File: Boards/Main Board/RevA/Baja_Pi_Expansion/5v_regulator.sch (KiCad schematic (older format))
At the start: 3 parts

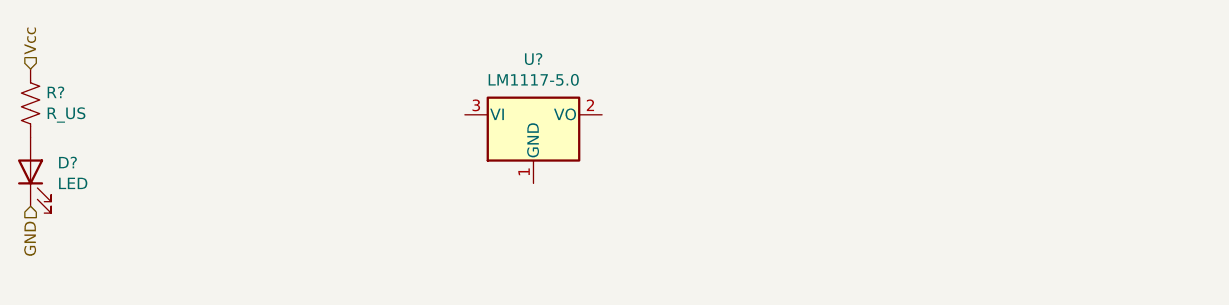
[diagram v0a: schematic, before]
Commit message: Added 5V Regulator Schematic
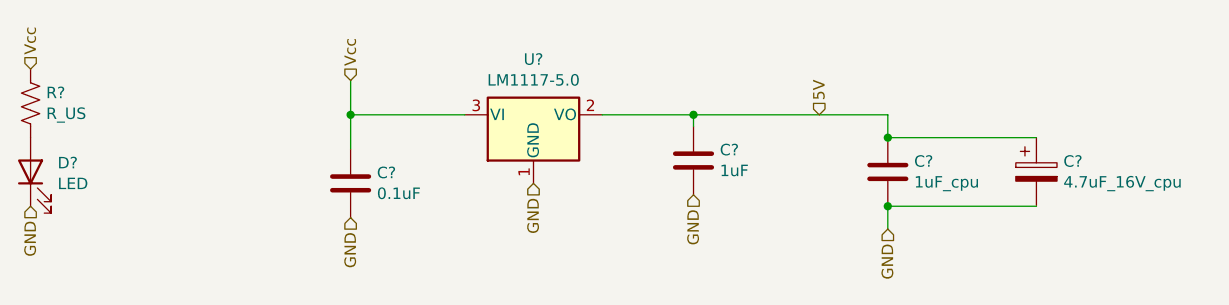
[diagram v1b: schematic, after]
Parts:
- added C?: 0.1uF, symbol Device:C
- added C?: 1uF, symbol Device:C
- added C?: 1uF_cpu, symbol Device:C
- added C?: 4.7uF_16V_cpu, symbol Device:CP
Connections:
- net GND: now also U?.1 (GND), C?.2, C?.2, C?.2, C?.2
- net Vcc: now also U?.3 (VI), C?.1
- net 5V: now reaches U?.2 (VO)
- net 5V: now also C?.1, C?.1, C?.1
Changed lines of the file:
@@
 	1    0    0    -1
 $EndComp
+$Comp
+L Device:C C?
+U 1 1 61655F33
+P 3950 3150
+F 0 "C?" H 4065 3196 50  0000 L CNN
+F 1 "0.1uF" H 4065 3105 50  0000 L CNN
+F 2 "" H 3988 3000 50  0001 C CNN
+F 3 "~" H 3950 3150 50  0001 C CNN
+	1    3950 3150
+	1    0    0    -1
+$EndComp
+$Comp
+L Device:C C?
+U 1 1 61656877
+P 5450 3050
+F 0 "C?" H 5565 3096 50  0000 L CNN
+F 1 "1uF" H 5565 3005 50  0000 L CNN
+F 2 "" H 5488 2900 50  0001 C CNN
+F 3 "~" H 5450 3050 50  0001 C CNN
+	1    5450 3050
+	1    0    0    -1
+$EndComp
+$Comp
+L Device:C C?
+U 1 1 6165740F
+P 6300 3100
+F 0 "C?" H 6415 3146 50  0000 L CNN
+F 1 "1uF_cpu" H 6415 3055 50  0000 L CNN
+F 2 "" H 6338 2950 50  0001 C CNN
+F 3 "~" H 6300 3100 50  0001 C CNN
+	1    6300 3100
+	1    0    0    -1
+$EndComp
+$Comp
+L Device:CP C?
+U 1 1 6165888C
+P 6950 3100
+F 0 "C?" H 7068 3146 50  0000 L CNN
+F 1 "4.7uF_16V_cpu" H 7068 3055 50  0000 L CNN
+F 2 "" H 6988 2950 50  0001 C CNN
+F 3 "~" H 6950 3100 50  0001 C CNN
+	1    6950 3100
+	1    0    0    -1
+$EndComp
+Wire Wire Line
+	5450 2900 5450 2850
+Wire Wire Line
+	5450 2850 5050 2850
+Text HLabel 5450 3200 3    50   Input ~ 0
+GND
+Text HLabel 3950 2700 1    50   Input ~ 0
+Vcc
+Text HLabel 3950 3300 3    50   Input ~ 0
+GND
+Wire Wire Line
+	4450 2850 3950 2850
+Wire Wire Line
+	3950 2850 3950 2700
+Wire Wire Line
+	3950 3000 3950 2850
+Connection ~ 3950 2850
+Text HLabel 6300 3350 3    50   Input ~ 0
+GND
+Wire Wire Line
+	6300 3350 6300 3250
+Wire Wire Line
+	5450 2850 6300 2850
+Wire Wire Line
+	6300 2850 6300 2950
+Connection ~ 5450 2850
+Wire Wire Line
+	6300 2950 6950 2950
+Connection ~ 6300 2950
+Wire Wire Line
+	6300 3250 6950 3250
+Connection ~ 6300 3250
+Text HLabel 4750 3150 3    50   Input ~ 0
+GND
+Text HLabel 6000 2850 1    50   Input ~ 0
+5V
 $EndSCHEMATC
